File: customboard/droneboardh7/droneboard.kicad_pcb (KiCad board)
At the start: 4 copper layers, 38 x 38 mm, 56 parts, among them J1 Conn_01x04, J2 Conn_01x04, J3 Conn_01x05_Pin, J4 Conn_01x02_Pin, J5 USB_C_Receptacle_USB2.0_16P, J6 Conn_01x04, SW1 SW_Push, SW2 SW_Push, U2 STM32H723VGTx, U3 L78M05CDT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

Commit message: board work
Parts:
- added J7: Conn_01x01_Pin, TestPoint:TestPoint_Pad_2.5x2.5mm, B.Cu at (85.2, 97.0)
- added J8: Conn_01x01_Pin, TestPoint:TestPoint_Pad_2.5x2.5mm, B.Cu at (85.2, 100.7)
- added J9: Conn_01x01_Pin, TestPoint:TestPoint_Pad_2.5x2.5mm, B.Cu at (85.2, 104.3)
- J4: footprint Connector_PinHeader_1.27mm:PinHeader_1x02_P1.27mm_Vertical -> Connector_PinHeader_2.54mm:PinHeader_1x02_P2.54mm_Vertical
- moved J4 1.48 mm to (61.9, 84.8)
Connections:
- U2 pad 72: unconnected-(U2-PA13(JTMS-Pad72) -> /SWDIO
- U2 pad 76: unconnected-(U2-PA14(JTCK-Pad76) -> /SWCLK
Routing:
- net /SWDIO: track 0.00 -> 12.8 mm, vias 0 -> 1
- net /SWCLK: track 0.00 -> 11.0 mm, vias 0 -> 1
- net /GND: track 154.5 -> 148.6 mm
- net /12V: track 8.47 -> 11.4 mm
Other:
- board text added: "SWCLK"
- board text added: "SWDIO"
- board text added: "VBAT"

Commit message: h7 hardware done
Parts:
- R7, R8: footprint Resistor_SMD:R_0402_1005Metric -> Resistor_SMD:R_0603_1608Metric
- U3: value L78M05CDT -> LM7805MPX; footprint Package_TO_SOT_SMD:TO-252-2 -> Package_TO_SOT_SMD:SOT-223-3_TabPin2
- U5, U6: value LDK130M33R -> SPX3819M5-L-3-3
- moved R1 15.6 mm to (54.6, 103.8), turned to 0 degrees
- moved U4 12.0 mm to (67.0, 95.0)
- moved C21 12.0 mm to (64.5, 92.4)
- moved C22 12.0 mm to (69.5, 92.0)
- moved C1 12.0 mm to (64.9, 94.7)
- moved C2 12.0 mm to (64.5, 93.5)
- moved C4 12.0 mm to (69.1, 94.4)
- moved U5 12.0 mm to (66.9, 91.4)
- moved J1 11.3 mm to (51.9, 109.9), turned to 90 degrees
- moved C23 10.2 mm to (64.4, 90.2), turned to -90 degrees
- moved J2 9.68 mm to (51.9, 106.8), turned to 90 degrees
- moved R9 7.94 mm to (71.6, 96.7), turned to 0 degrees
- moved R2 7.89 mm to (58.4, 112.3)
- moved J6 7.74 mm to (60.8, 117.9), turned to 90 degrees
- moved C24 7.54 mm to (59.6, 90.7), turned to -90 degrees
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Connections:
- J5 pad A5: unconnected-(J5-CC1-PadA5) -> Net-(J5-CC1)
- J5 pad A8: Net-(J5-SBU1) -> unconnected-(J5-SBU1-PadA8)
- J5 pad B5: unconnected-(J5-CC2-PadB5) -> Net-(J5-CC2)
- J5 pad B8: Net-(J5-SBU2) -> unconnected-(J5-SBU2-PadB8)
- R10 pad 1: Net-(J5-SBU1) -> Net-(J5-CC1)
- R11 pad 1: Net-(J5-SBU2) -> Net-(J5-CC2)
- U2 pad 1: /SCK -> /GREEN
- U2 pad 15: /BLUE -> unconnected-(U2-PC0-Pad15)
- U2 pad 16: /YELLOW -> unconnected-(U2-PC1-Pad16)
- U2 pad 2: unconnected-(U2-PE3-Pad2) -> /BLUE
- U2 pad 20: unconnected-(U2-VREF+-Pad20) -> /VMCU
- U2 pad 3: unconnected-(U2-PE4-Pad3) -> /YELLOW
- U2 pad 4: /MISO -> unconnected-(U2-PE5-Pad4)
- U2 pad 5: /MOSI -> unconnected-(U2-PE6-Pad5)
- U2 pad 7: /GREEN -> unconnected-(U2-PC13-Pad7)
- U2 pad 8: /IMU_CS -> unconnected-(U2-PC14-Pad8)
- U2 pad 89: unconnected-(U2-PB3(JTDO-Pad89) -> /SCK
- U2 pad 90: unconnected-(U2-PB4(NJTRST)-Pad90) -> /MISO
- U2 pad 91: unconnected-(U2-PB5-Pad91) -> /MOSI
- U2 pad 93: unconnected-(U2-PB7-Pad93) -> /IMU_CS
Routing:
- net /MOSI: track 11.8 -> 2.35 mm, vias 2 -> 0
- net /5V: track 60.1 -> 68.7 mm
- net /IMU_CS: track 10.6 -> 2.35 mm, vias 2 -> 0
- net /SCK: track 13.3 -> 5.90 mm
- net /GREEN: track 11.4 -> 5.06 mm, vias 2 -> 0
- net /MISO: track 8.35 -> 2.54 mm, vias 2 -> 0
- net /BLUE: track 10.2 -> 4.83 mm, vias 2 -> 0
- net /RESET1: track 27.9 -> 22.5 mm
- net /U2TX: track 11.4 -> 6.48 mm
- net /YELLOW: track 9.55 -> 5.22 mm, vias 2 -> 0
- net /U7RX: track 12.0 -> 7.70 mm
- net /VBATMON: track 27.1 -> 30.8 mm
- net /U4TX: track 13.1 -> 9.55 mm, vias 0 -> 1
- net /U2RX: track 11.3 -> 8.25 mm
- net /MOTOR3: track 7.03 -> 4.72 mm
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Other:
- board text added: "5"
- board text added: "BAT"
- board text added: "T"
- board text removed: "5V"
- board text removed: "RX"
- board text removed: "TX"
- board text removed: "VBAT"

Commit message: smps initial
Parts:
- removed C19: 330n, Capacitor_SMD:C_0805_2012Metric
- removed C20: 100n, Capacitor_SMD:C_0603_1608Metric
- removed U3: LM7805MPX, Package_TO_SOT_SMD:SOT-223-3_TabPin2
- added C13: 10u, Capacitor_SMD:C_1206_3216Metric, B.Cu at (56.5, 93.2)
- added C14: 100n, Capacitor_SMD:C_0603_1608Metric, B.Cu at (54.4, 99.9)
- added C17: 22u, Capacitor_SMD:C_0805_2012Metric, B.Cu at (52.1, 104.1)
- added C18: 22u, Capacitor_SMD:C_0805_2012Metric, B.Cu at (54.2, 104.1)
- added L1: IFSC2020DZER4R7N01, Inductor_SMD:L_Vishay_IHLP-2020, B.Cu at (58.0, 102.4)
- added U1: AP63205WU, Package_TO_SOT_SMD:TSOT-23-6, B.Cu at (58.0, 96.5)
- moved J4 13.4 mm to (52.5, 94.4), turned to 180 degrees
- moved D2 4.54 mm to (75.7, 86.6)
- moved R4 4.36 mm to (72.7, 86.5)
- moved R7 4.12 mm to (59.5, 87.4), turned to 0 degrees
- moved C1 1.68 mm to (64.9, 93.0)
- moved C2 1.68 mm to (64.5, 91.9)
- moved C21 1.68 mm to (64.5, 90.7)
- moved C22 1.68 mm to (69.5, 90.3)
- moved C23 1.68 mm to (64.4, 88.5)
- moved C4 1.68 mm to (69.1, 92.8)
- moved U4 1.68 mm to (67.0, 93.3)
- moved U5 1.68 mm to (66.9, 89.8)
- moved R8 1.55 mm to (59.5, 85.8)
- moved R1 0.28 mm to (54.6, 104.0)
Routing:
- net /GND: track 150.8 -> 237.9 mm, vias 39 -> 33
- net /5V: track 68.7 -> 124.7 mm, vias 1 -> 3
- net /12V: track 10.6 -> 47.4 mm
- net Net-(U1-SW): track 0.00 -> 20.4 mm
- net Net-(U1-BST): track 0.00 -> 6.39 mm
- net /VGYRO: track 11.9 -> 14.2 mm
- net /MOSI: track 2.35 -> 4.04 mm
- net /IMU_CS: track 2.35 -> 4.04 mm
- net /MISO: track 2.54 -> 4.22 mm
- net /SCK: track 5.90 -> 7.58 mm
- net /BOOT: track 20.9 -> 21.5 mm
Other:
- board text removed: "+"
- board text removed: "-"
- board text removed: "BAT"

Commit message: smps complete
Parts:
- removed J7, J8, J9: Conn_01x01_Pin, TestPoint:TestPoint_Pad_2.5x2.5mm
- added J10: Conn_01x03_Pin, Connector_PinHeader_2.54mm:PinHeader_1x03_P2.54mm_Vertical, F.Cu at (75.2, 89.5)
- L1: value IFSC2020DZER4R7N01 -> IHLP2020CZER4R7M11
- moved R1 6.13 mm to (57.4, 109.5), turned to -90 degrees
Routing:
- net /GND: track 237.9 -> 270.5 mm, vias 33 -> 34
- net /5V: track 124.7 -> 132.9 mm
- net /SWCLK: track 10.7 -> 3.74 mm, vias 1 -> 0
- net /VMCU: track 50.2 -> 46.3 mm
- net /U4RX: track 12.1 -> 10.2 mm, vias 1 -> 2
- net /SWDIO: track 11.3 -> 12.5 mm, vias 1 -> 2
- net /BOOT: track 21.5 -> 22.4 mm
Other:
- board text added: "+"
- board text added: "CLK"
- board text added: "DIO"

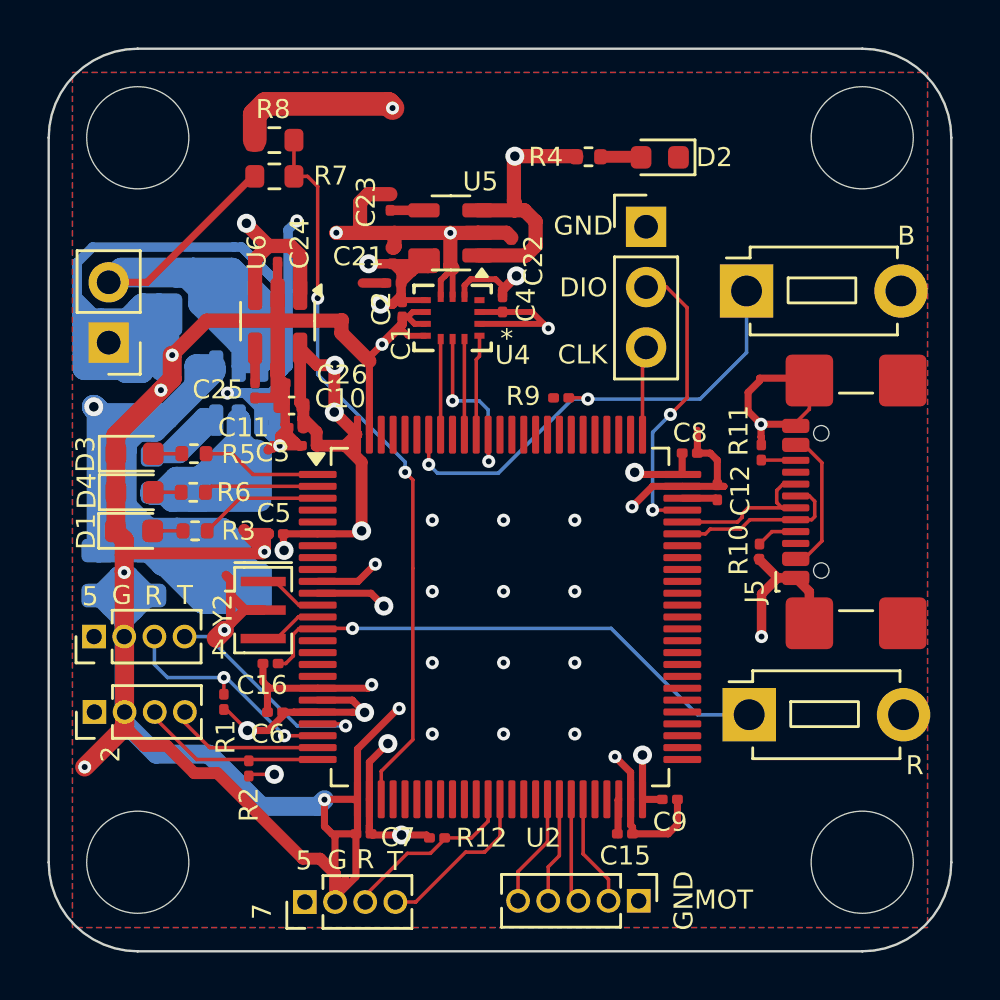
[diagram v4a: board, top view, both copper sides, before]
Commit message: smps pcb; bom
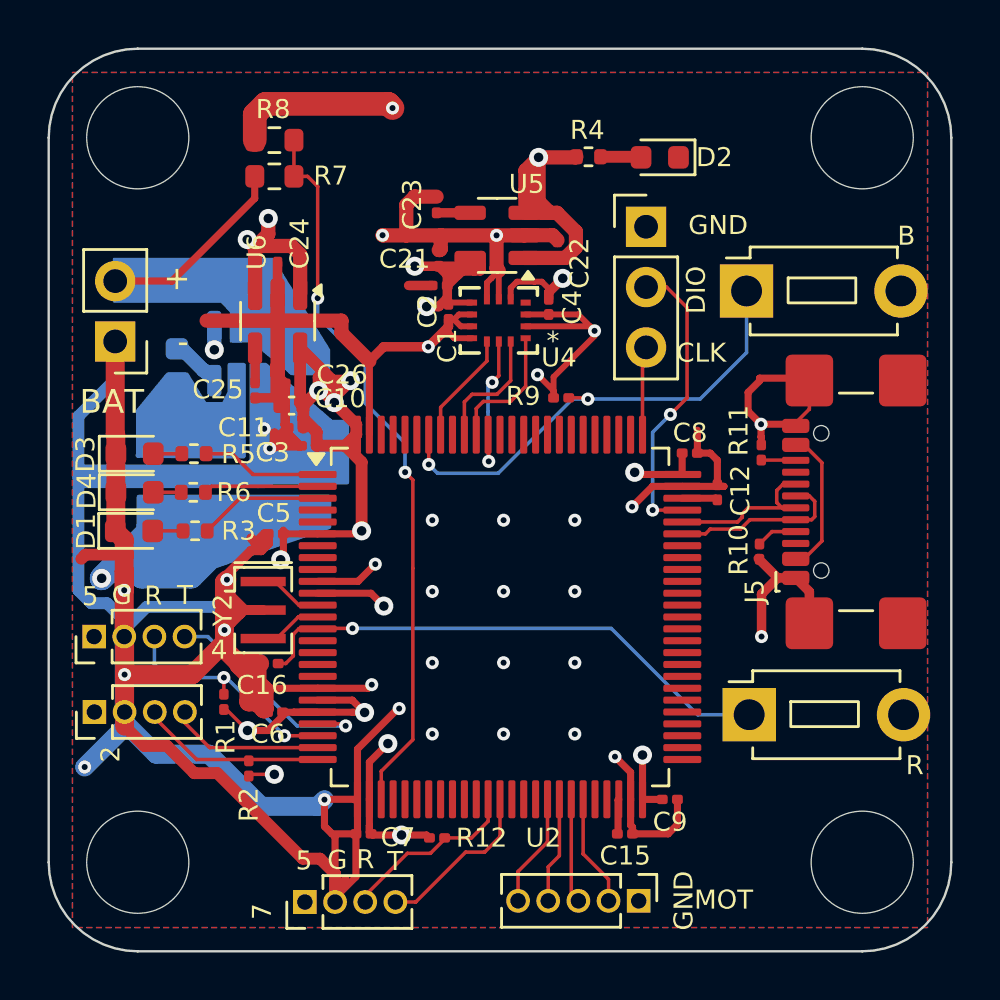
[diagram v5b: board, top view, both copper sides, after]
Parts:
- moved C17 7.71 mm to (59.0, 100.7), turned to 90 degrees
- moved C18 7.65 mm to (61.1, 100.7), turned to 90 degrees
- moved C13 5.58 mm to (60.9, 96.6), turned to -90 degrees
- moved C14 4.63 mm to (55.4, 95.4)
- moved L1 3.34 mm to (55.2, 100.6)
- moved C2 1.95 mm to (66.5, 92.0)
- moved C21 1.95 mm to (66.4, 90.8)
- moved C22 1.95 mm to (71.4, 90.4)
- moved U4 1.95 mm to (69.0, 93.4)
- moved C1 1.95 mm to (66.8, 93.1)
- moved C23 1.95 mm to (66.3, 88.6)
- moved C4 1.95 mm to (71.1, 92.9)
- moved U5 1.95 mm to (68.9, 89.9)
- moved U1 1.66 mm to (57.9, 94.8)
- moved J4 0.28 mm to (52.8, 94.3)
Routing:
- net /5V: track 132.9 -> 81.7 mm, vias 3 -> 5
- net /GND: track 270.5 -> 229.5 mm, vias 34 -> 33
- net /12V: track 47.4 -> 8.24 mm
- net Net-(U1-SW): track 20.4 -> 0.00 mm
- net /VMCU: track 46.3 -> 51.8 mm, vias 12 -> 13
- net Net-(U1-BST): track 6.39 -> 2.37 mm
- net /MISO: track 4.22 -> 5.60 mm
- net /MOSI: track 4.04 -> 5.36 mm
- net /SCK: track 7.58 -> 6.38 mm
- net /IMU_CS: track 4.04 -> 4.74 mm
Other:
- board text added: "-"
- board text added: "BAT"

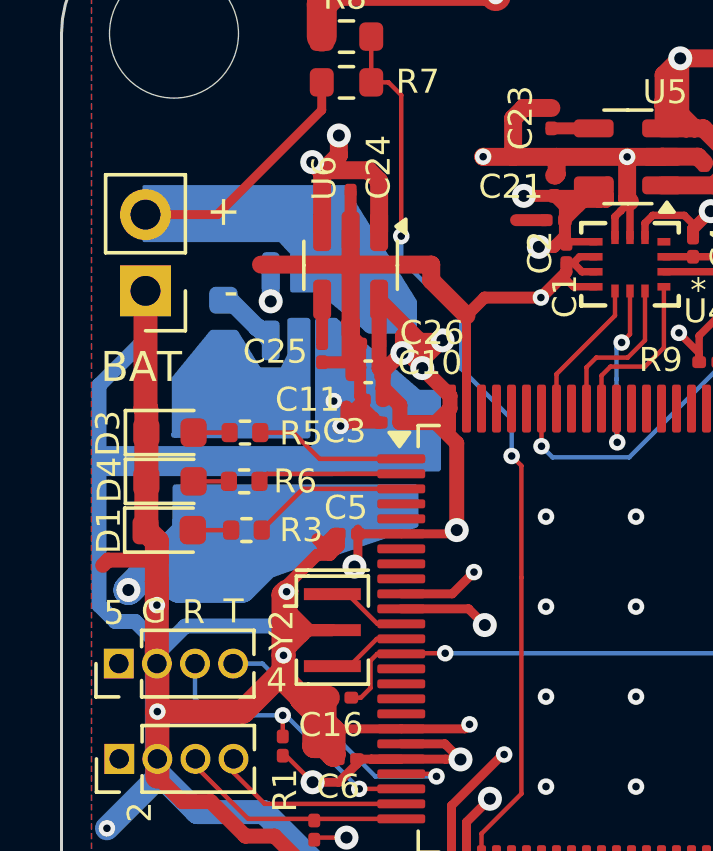
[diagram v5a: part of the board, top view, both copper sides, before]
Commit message: SMA TOP; 20mm VTX; 3A SMPS; MSP OSD
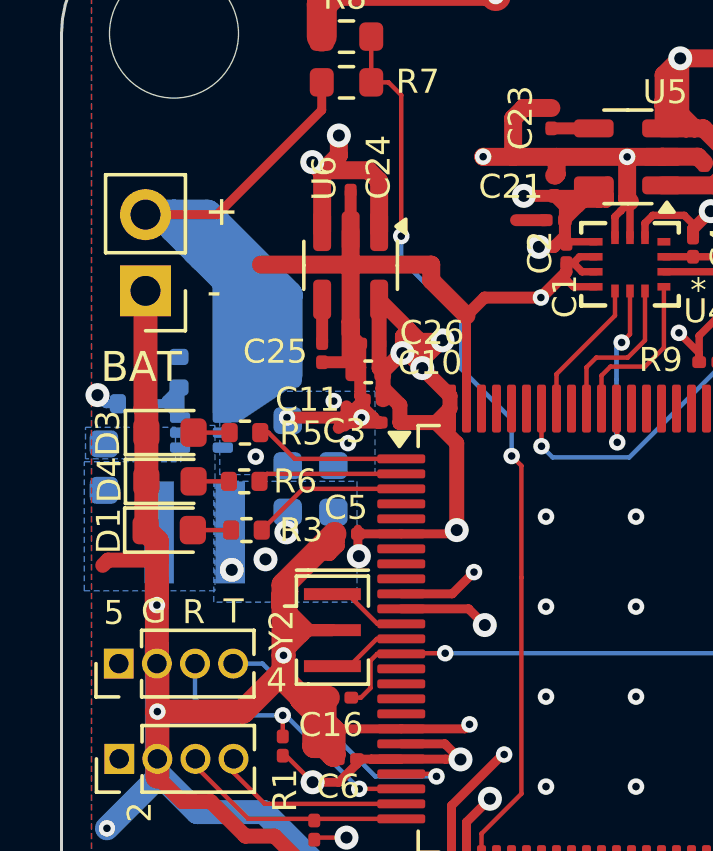
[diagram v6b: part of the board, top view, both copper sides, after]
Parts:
- added R13: 1K, Resistor_SMD:R_0402_1005Metric, B.Cu at (53.9, 97.0)
- added R14: 5.49K, Resistor_SMD:R_0402_1005Metric, B.Cu at (52.4, 98.1)
- C13: footprint Capacitor_SMD:C_1206_3216Metric -> Capacitor_SMD:C_0603_1608Metric
- C17, C18: footprint Capacitor_SMD:C_0805_2012Metric -> Capacitor_SMD:C_0603_1608Metric
- L1: value IHLP2020CZER4R7M11 -> XEL4030-332MEC; footprint Inductor_SMD:L_Vishay_IHLP-2020 -> Inductor_SMD:L_Coilcraft_XxL4030
- U1: value AP63205WU -> AP62300Z6; footprint Package_TO_SOT_SMD:TSOT-23-6 -> Package_TO_SOT_SMD:SOT-563
- moved C14 6.23 mm to (51.4, 100.2)
- moved U1 5.33 mm to (54.7, 99.0), turned to 180 degrees
- moved C13 3.60 mm to (57.5, 97.9)
- moved C18 2.04 mm to (59.1, 100.9)
- moved L1 1.90 mm to (54.4, 102.4), turned to 0 degrees
- moved C17 1.52 mm to (57.5, 100.9)
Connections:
- C14 pad 1: Net-(U1-BST) -> /SMPS_BOOST
- C14 pad 2: Net-(U1-SW) -> /SMPS_V
- L1 pad 1: Net-(U1-SW) -> /SMPS_V
- U1 pad 1: /5V -> /12V
- U1 pad 2: /12V -> /SMPS_V
- U1 pad 3: /12V -> /GND
- U1 pad 4: /GND -> /SMPS_BOOST
- U1 pad 5: Net-(U1-SW) -> unconnected-(U1-EN-Pad5)
- U1 pad 6: Net-(U1-BST) -> Net-(U1-FB)
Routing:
- net /GND: track 229.5 -> 205.2 mm, vias 33 -> 35
- net /12V: track 8.24 -> 22.2 mm
- net /5V: track 81.7 -> 77.2 mm, vias 5 -> 7
- net Net-(U1-FB): track 0.00 -> 3.60 mm
- net Net-(U1-BST): track 2.37 -> 0.00 mm
- net /SMPS_V: track 0.00 -> 1.51 mm
- added copper zone on B.Cu, net /5V
- added copper zone on In2.Cu, net /5V
- added copper zone on B.Cu, net /SMPS_BOOST
- added copper zone on B.Cu, net /SMPS_V

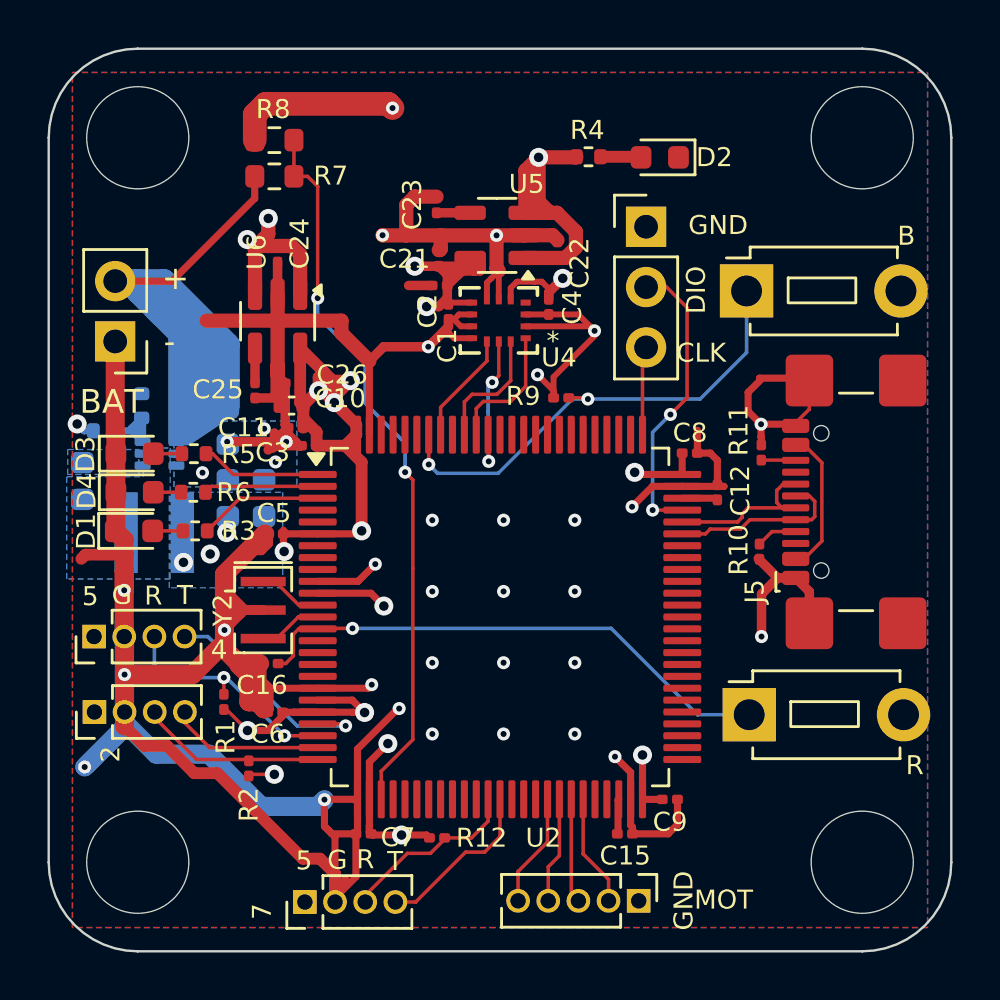
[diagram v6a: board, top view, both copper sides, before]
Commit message: battery/telemetry separation, parallel dshot, wider pin headers
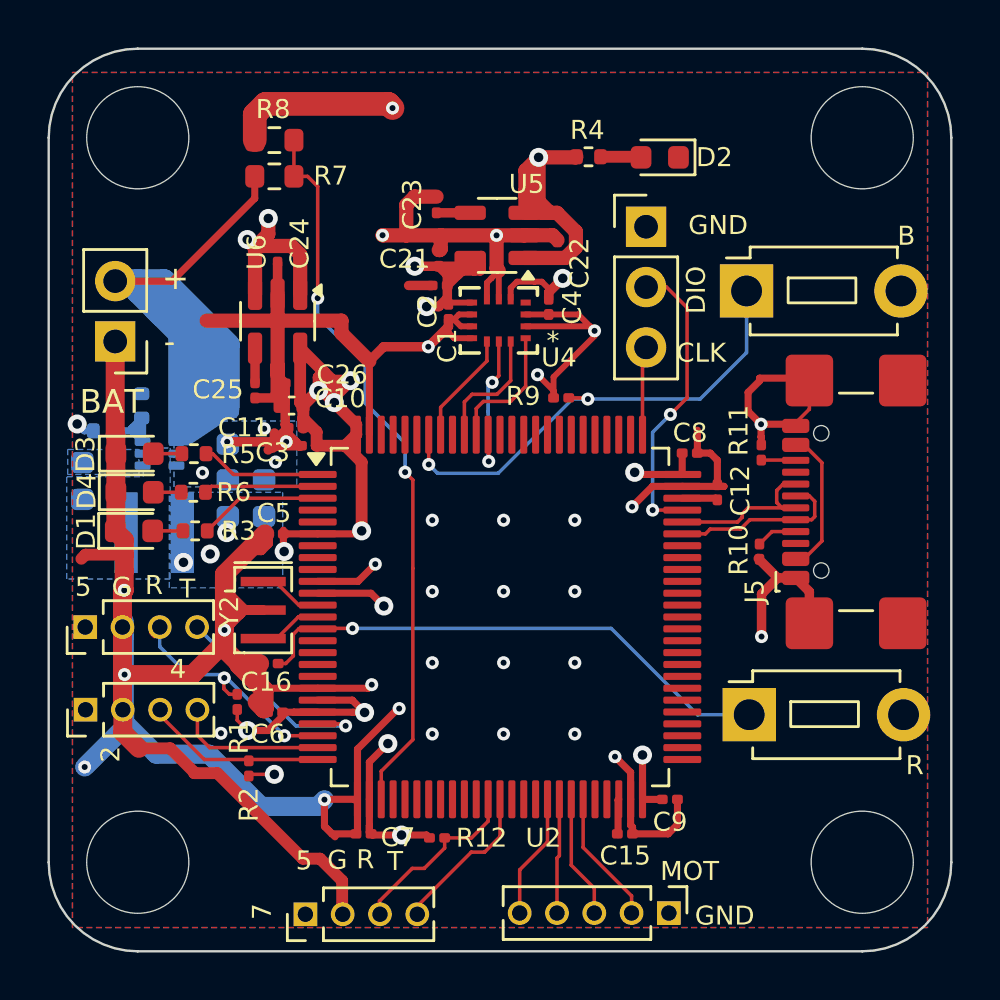
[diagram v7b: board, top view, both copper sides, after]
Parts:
- J1, J2, J6: footprint Connector_PinHeader_1.27mm:PinHeader_1x04_P1.27mm_Vertical -> Custom:PinHeaderWide4x
- J3: footprint Connector_PinHeader_1.27mm:PinHeader_1x05_P1.27mm_Vertical -> Custom:PinHeaderWide5x
- moved J3 1.37 mm to (76.1, 118.4)
- moved R1 0.56 mm to (57.9, 109.5)
- moved J2 0.55 mm to (51.5, 106.3)
- moved J6 0.52 mm to (60.8, 118.4)
- moved J1 0.39 mm to (51.6, 109.8)
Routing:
- net /GND: track 205.2 -> 196.7 mm, vias 35 -> 36
- net /MOTOR3: track 4.72 -> 5.63 mm
- net /5V: track 77.2 -> 78.1 mm
- net /MOTOR2: track 4.40 -> 5.19 mm

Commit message: h723 further work
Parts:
- C13: value 10u -> 10u25VX7R; footprint Capacitor_SMD:C_0603_1608Metric -> Capacitor_SMD:C_1210_3225Metric
- C14: value 100n -> 100n25VX7R
- C17, C18: value 22u -> 22u10VX5R; footprint Capacitor_SMD:C_0603_1608Metric -> Capacitor_SMD:C_0805_2012Metric
- J3: footprint Custom:PinHeaderWide5x -> Connector_PinHeader_2.00mm:PinHeader_1x05_P2.00mm_Vertical
- moved J3 1.44 mm to (77.5, 118.5)
- moved C13 1.00 mm to (58.2, 97.1)
- moved C18 0.62 mm to (59.7, 101.1)
- moved C17 0.22 mm to (57.7, 101.1)
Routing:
- net /12V: track 22.2 -> 8.24 mm
- net /GND: track 196.7 -> 198.2 mm, vias 36 -> 37
- net /MOTOR3: track 5.63 -> 6.57 mm
- net /YELLOW: track 5.22 -> 5.81 mm
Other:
- board text added: "M0"
- board text removed: "MOT"
- board text removed: "SWCLK"
- board text removed: "SWDIO"
